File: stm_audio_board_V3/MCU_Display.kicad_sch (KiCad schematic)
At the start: 16 parts, among them J10 USB_A, SW1 SW_SPST, U1 IS42S16100H-7TL, U7 STM32H723ZGTx, Y2 X1E0000210132

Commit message: minor changes
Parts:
- removed C15 (x2): 2.2uF, Capacitor_SMD:C_0805_2012Metric_Pad1.18x1.45mm_HandSolder, symbol Device:C_Polarized_Small_US
- removed J10: USB_A, Connector_USB:USB_A_CONNFLY_DS1095-WNR0, symbol Connector:USB_A
- removed R9 (x2): 1k, Resistor_SMD:R_0603_1608Metric_Pad0.98x0.95mm_HandSolder, symbol Device:R
- removed R9: 100R, Resistor_SMD:R_0603_1608Metric, symbol Device:R
- removed U1: IS42S16100H-7TL, Library:TSOP-2-50-new, symbol stm_audio:IS42S16100H-7TL
- added C15 (x2): 2.2uF, Capacitor_SMD:C_0805_2012Metric_Pad1.18x1.45mm_HandSolder, symbol Device:C_Polarized_Small_US
- added R9 (x2): 1k, Resistor_SMD:R_0603_1608Metric_Pad0.98x0.95mm_HandSolder, symbol Device:R
- added R9: 100R, Resistor_SMD:R_0603_1608Metric, symbol Device:R
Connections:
- net GND: now also C15.2, C15.2
- net LED1: now also R9.2
- net LED2: now also R9.2
- net at D10.2 (A): now also R9.1
- net at C37.2, Y2.3: now also R9.2
- net at U7.71 (VCAP): now also C15.1
- net at D11.2 (A): now also R9.1
- net at U7.106 (VCAP): now also C15.1
- net AD1939_SAI1A_CK: no longer names the net of U7.4 (PE5)
- net AD1939_SAI1A_SDO: no longer names the net of U7.5 (PE6)
- net AD1939_SAI1A_WS: no longer names the net of U7.3 (PE4)
- net AD1939_SAI1B_SDI: no longer names the net of U7.2 (PE3)
- net NRST renamed NRST_2
- net OSC0 renamed OSC0_2
- net OSC1 renamed OSC1_2
- net OSC1_2: now also R9.1
- net SWCLK_DSP renamed SWCLK_DISP
- net SWDIO_DSP renamed SWDIO_DISP
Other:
- note removed: "Wiring 1. Display SPI1 SPI2 touch interrupt etc 2. I2S 3. potmeters 4. external interrupt"
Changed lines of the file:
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@@
 (kicad_sch (version 20230121) (generator eeschema)
-  (paper "A3")
+  (paper "A2")

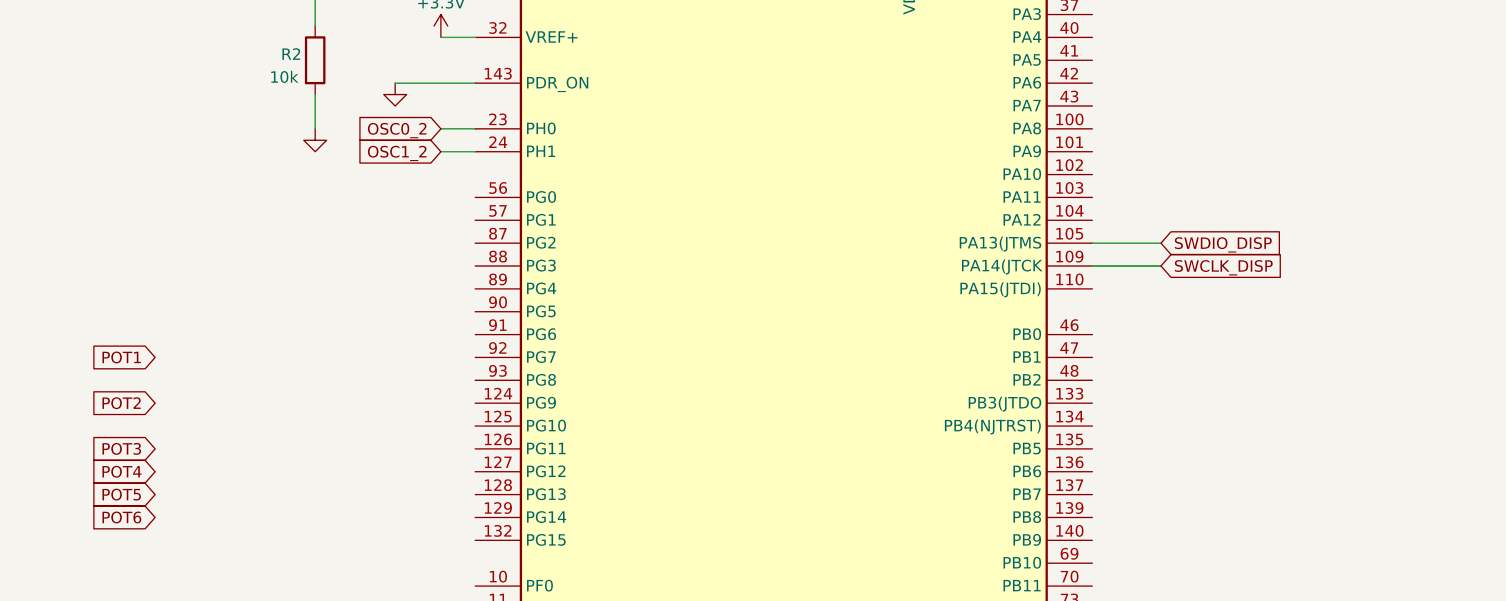
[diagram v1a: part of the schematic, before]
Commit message: New orientation, Overvoltage protection added
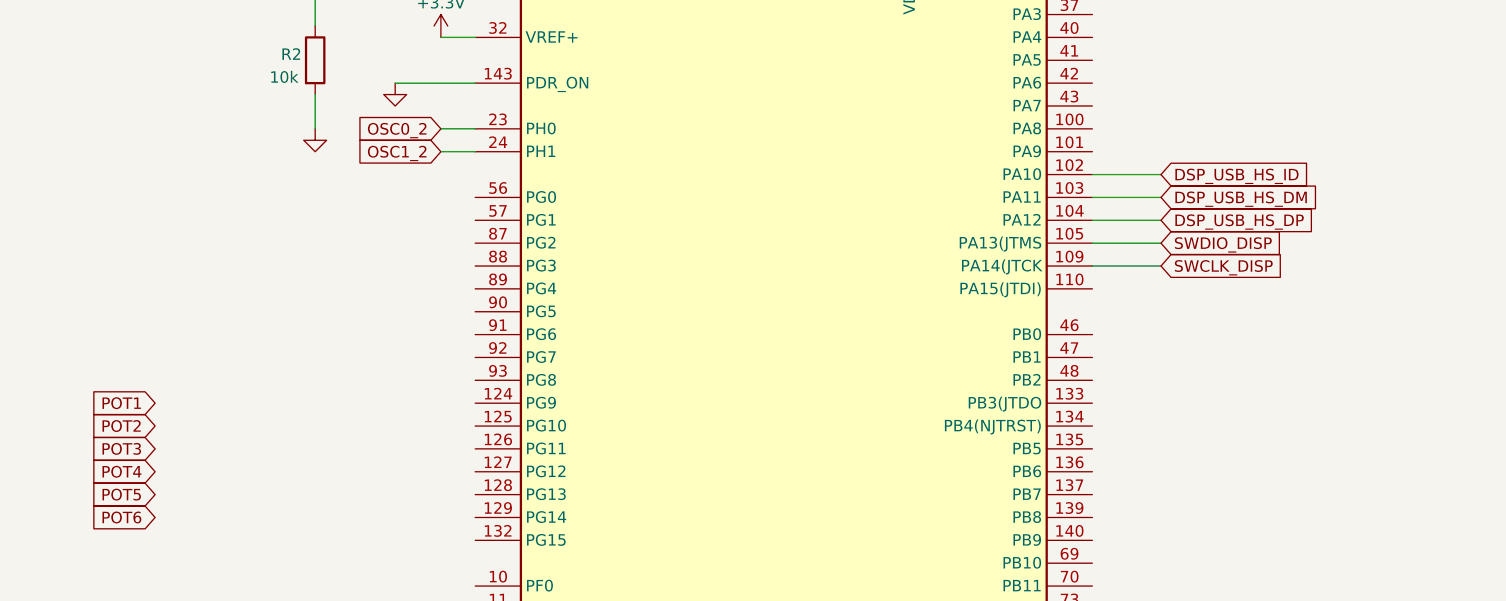
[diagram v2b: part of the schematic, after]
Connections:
- net DSP_USB_HS_ID: now reaches U7.102 (PA10)
- net DSP_USB_HS_DM: now reaches U7.103 (PA11)
- net DSP_USB_HS_DP: now reaches U7.104 (PA12)

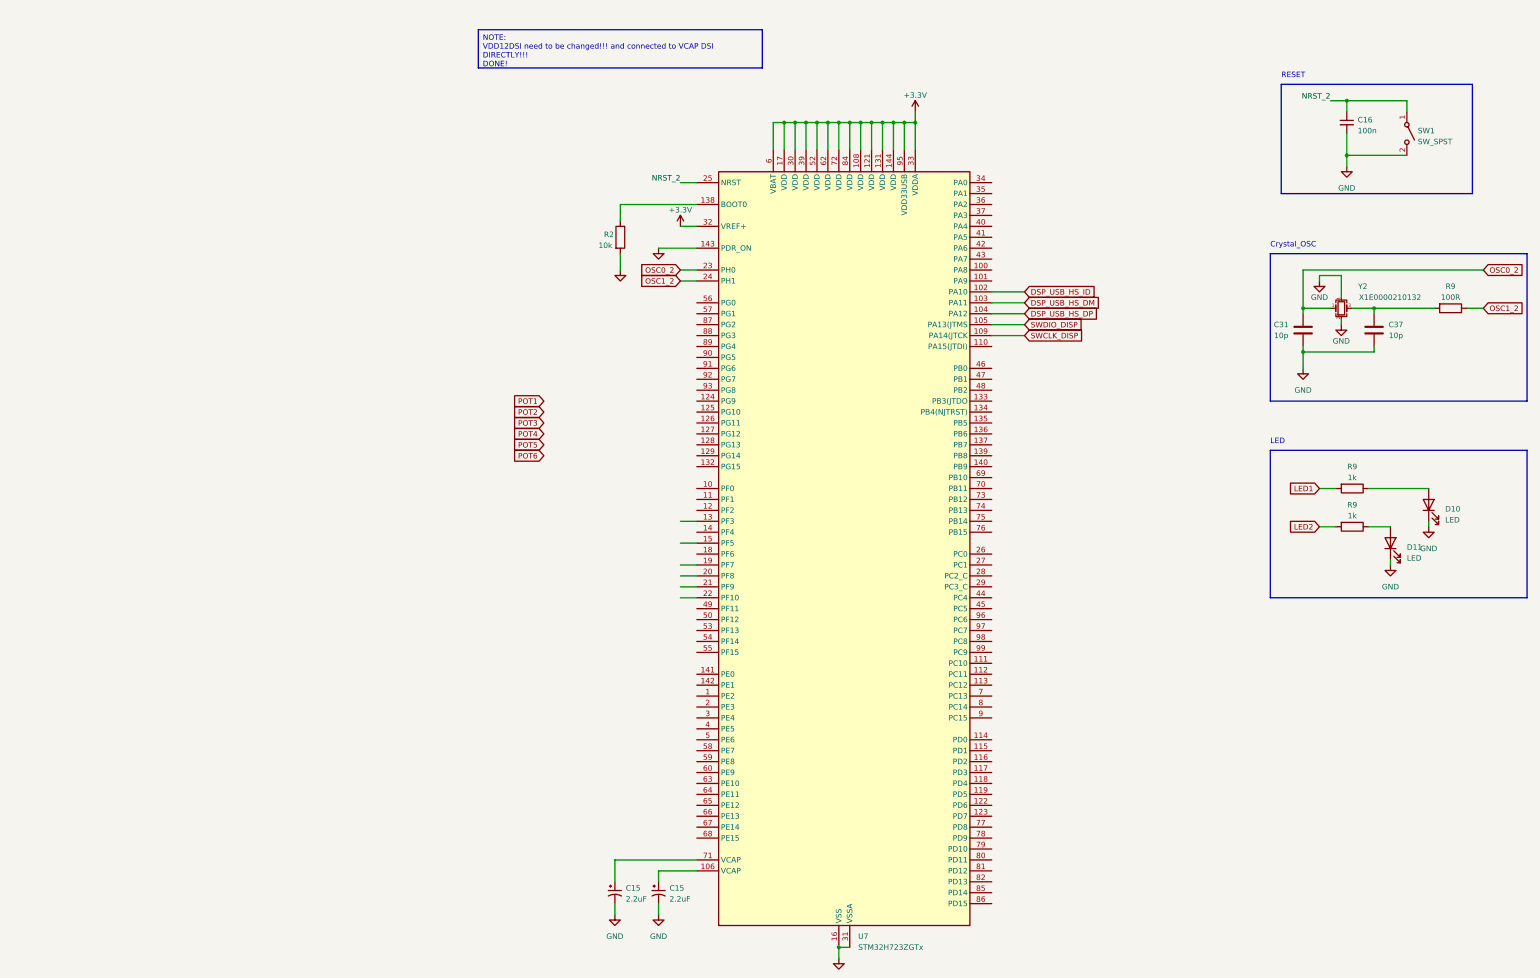
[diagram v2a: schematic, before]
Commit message: Testpoints and parts for usb hub added
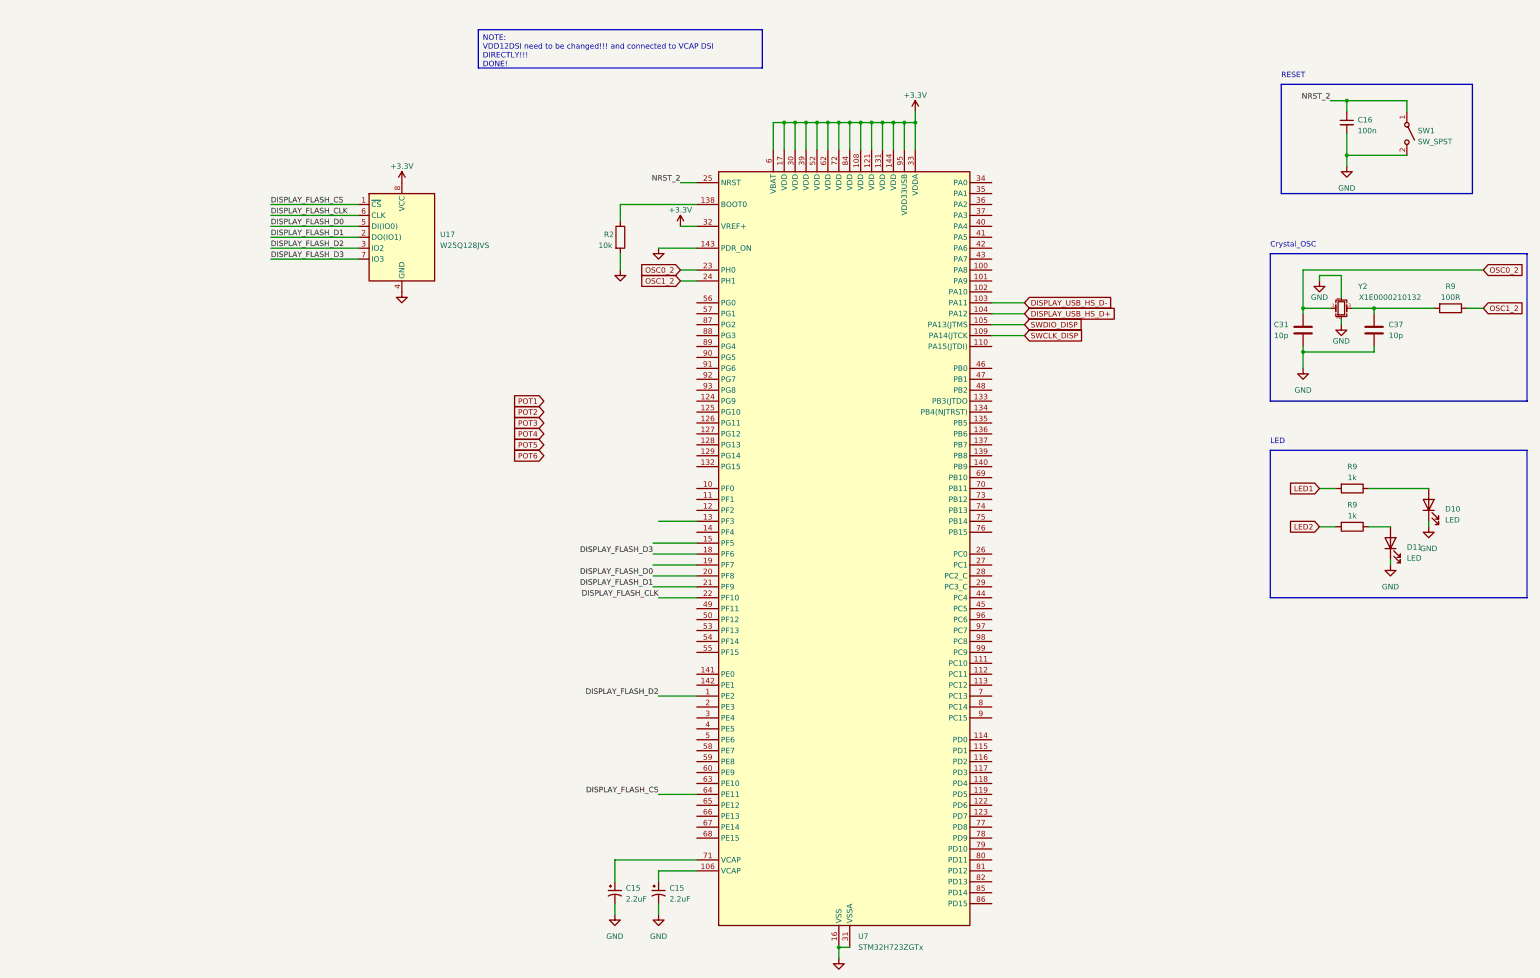
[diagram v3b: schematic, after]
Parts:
- added U17: W25Q128JVS, Package_SO:SOIC-8_5.23x5.23mm_P1.27mm, symbol Memory_Flash:W25Q128JVS
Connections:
- net +3.3V: now also U17.8 (VCC)
- net GND: now also U17.4 (GND)
- net DISPLAY_FLASH_D2: now reaches U7.1 (PE2)
- net DISPLAY_FLASH_D2: now also U17.3 (IO2)
- net DISPLAY_FLASH_D3: now reaches U7.18 (PF6)
- net DISPLAY_FLASH_D3: now also U17.7 (IO3)
- net DISPLAY_FLASH_D0: now reaches U7.20 (PF8)
- net DISPLAY_FLASH_D0: now also U17.5 (DI(IO0))
- net DISPLAY_FLASH_D1: now reaches U7.21 (PF9)
- net DISPLAY_FLASH_D1: now also U17.2 (DO(IO1))
- net DISPLAY_FLASH_CLK: now reaches U7.22 (PF10)
- net DISPLAY_FLASH_CLK: now also U17.6 (CLK)
- net DISPLAY_FLASH_CS: now reaches U7.64 (PE11)
- net DISPLAY_FLASH_CS: now also U17.1 (~{CS})
- net DSP_USB_HS_DM renamed DISPLAY_USB_HS_D-
- net DSP_USB_HS_DP renamed DISPLAY_USB_HS_D+
- net DSP_USB_HS_ID: no longer names the net of U7.102 (PA10)

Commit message: Reworked outline for enclosure
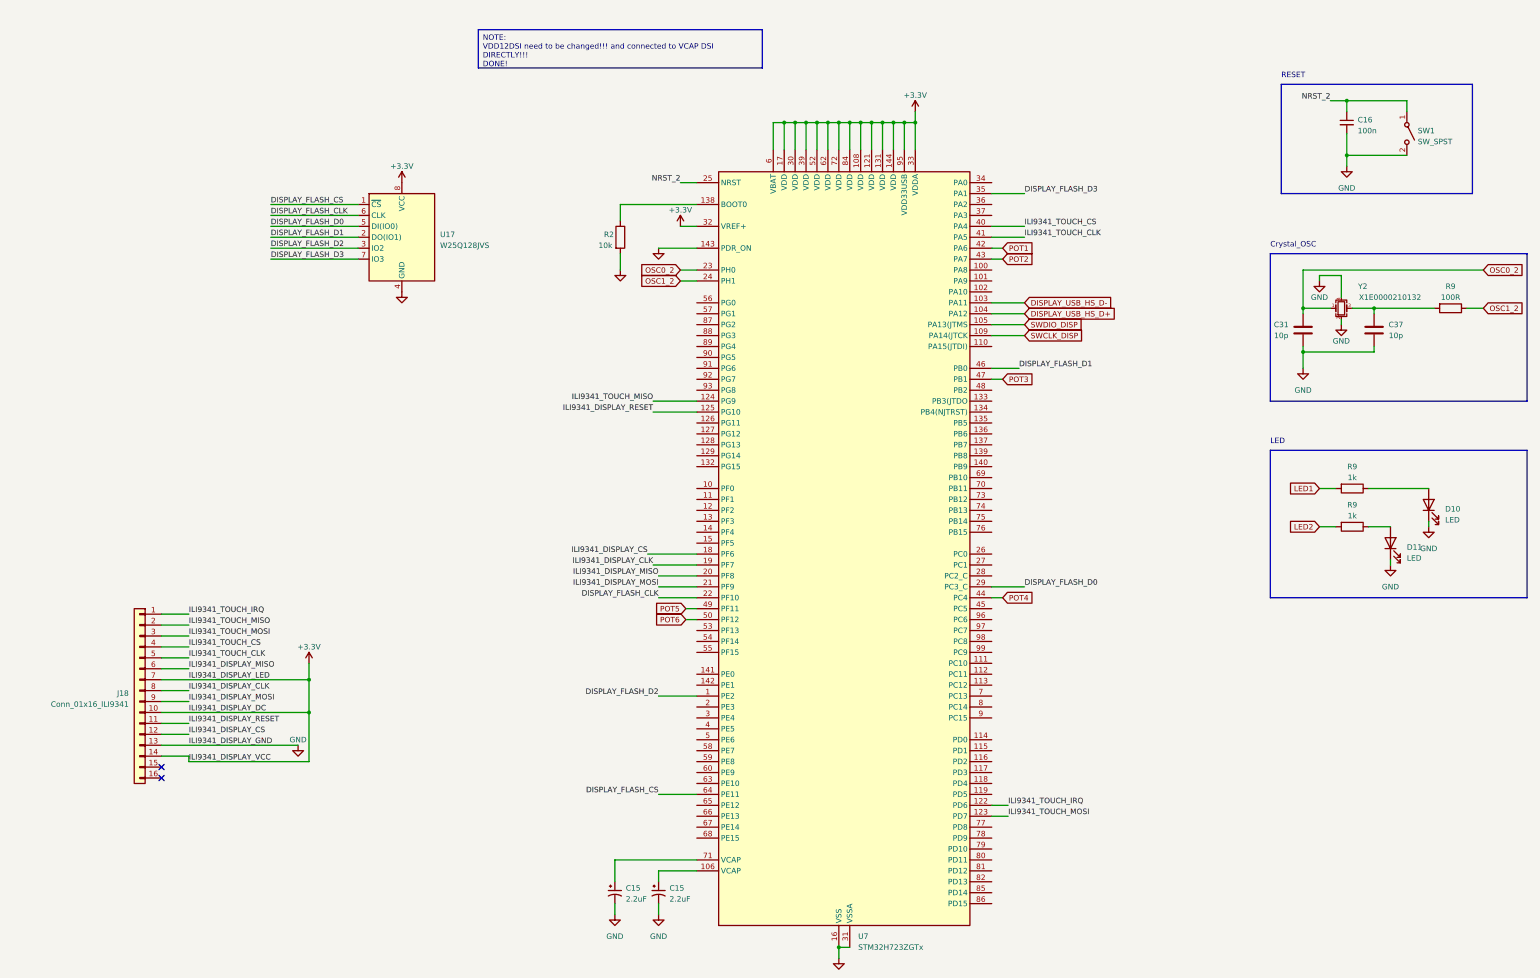
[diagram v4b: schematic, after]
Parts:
- added J18: Conn_01x16_ILI9341, Connector_PinHeader_2.54mm:PinHeader_1x16_P2.54mm_Vertical, symbol Connector_Generic:Conn_01x16
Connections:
- net +3.3V: now also J18.10 (Pin_10), J18.14 (Pin_14), J18.7 (Pin_7)
- net DISPLAY_FLASH_D0: now also U7.29 (PC3_C); no longer U7.20 (PF8)
- net DISPLAY_FLASH_D1: now also U7.46 (PB0); no longer U7.21 (PF9)
- net DISPLAY_FLASH_D3: now also U7.35 (PA1); no longer U7.18 (PF6)
- net GND: now also J18.13 (Pin_13)
- net POT1: now also U7.42 (PA6)
- net POT2: now also U7.43 (PA7)
- net POT3: now also U7.47 (PB1)
- net POT4: now also U7.44 (PC4)
- net POT5: now also U7.49 (PF11)
- net POT6: now also U7.50 (PF12)
- net ILI9341_TOUCH_IRQ: now reaches U7.122 (PD6)
- net ILI9341_TOUCH_IRQ: now also J18.1 (Pin_1)
- net ILI9341_TOUCH_MOSI: now reaches U7.123 (PD7)
- net ILI9341_TOUCH_MOSI: now also J18.3 (Pin_3)
- net ILI9341_TOUCH_MISO: now reaches U7.124 (PG9)
- net ILI9341_TOUCH_MISO: now also J18.2 (Pin_2)
- net ILI9341_DISPLAY_RESET: now reaches U7.125 (PG10)
- net ILI9341_DISPLAY_RESET: now also J18.11 (Pin_11)
- net ILI9341_DISPLAY_CLK: now reaches U7.19 (PF7)
- net ILI9341_DISPLAY_CLK: now also J18.8 (Pin_8)
- net ILI9341_TOUCH_CS: now reaches U7.40 (PA4)
- net ILI9341_TOUCH_CS: now also J18.4 (Pin_4)
- net ILI9341_TOUCH_CLK: now reaches U7.41 (PA5)
- net ILI9341_TOUCH_CLK: now also J18.5 (Pin_5)
- new net ILI9341_DISPLAY_CS: J18.12 (Pin_12), U7.18 (PF6)
- new net ILI9341_DISPLAY_MISO: J18.6 (Pin_6), U7.20 (PF8)
- new net ILI9341_DISPLAY_MOSI: J18.9 (Pin_9), U7.21 (PF9)
- no-connect marks 0 -> 2
